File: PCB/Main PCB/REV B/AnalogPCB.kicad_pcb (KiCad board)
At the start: 2 copper layers, 60 x 100 mm, 60 parts, among them J1 DF12NB_4.0_-20DP-0.5V_51_, J2 393570002, J3 393570002, J4 393570002, J5 393570002, J6 SJ3-35053D, Q1 2N7002, Q2 2N7002, Q3 2N7002, U1 ALDP105W, U2 ALDP105W, U3 ALDP105W

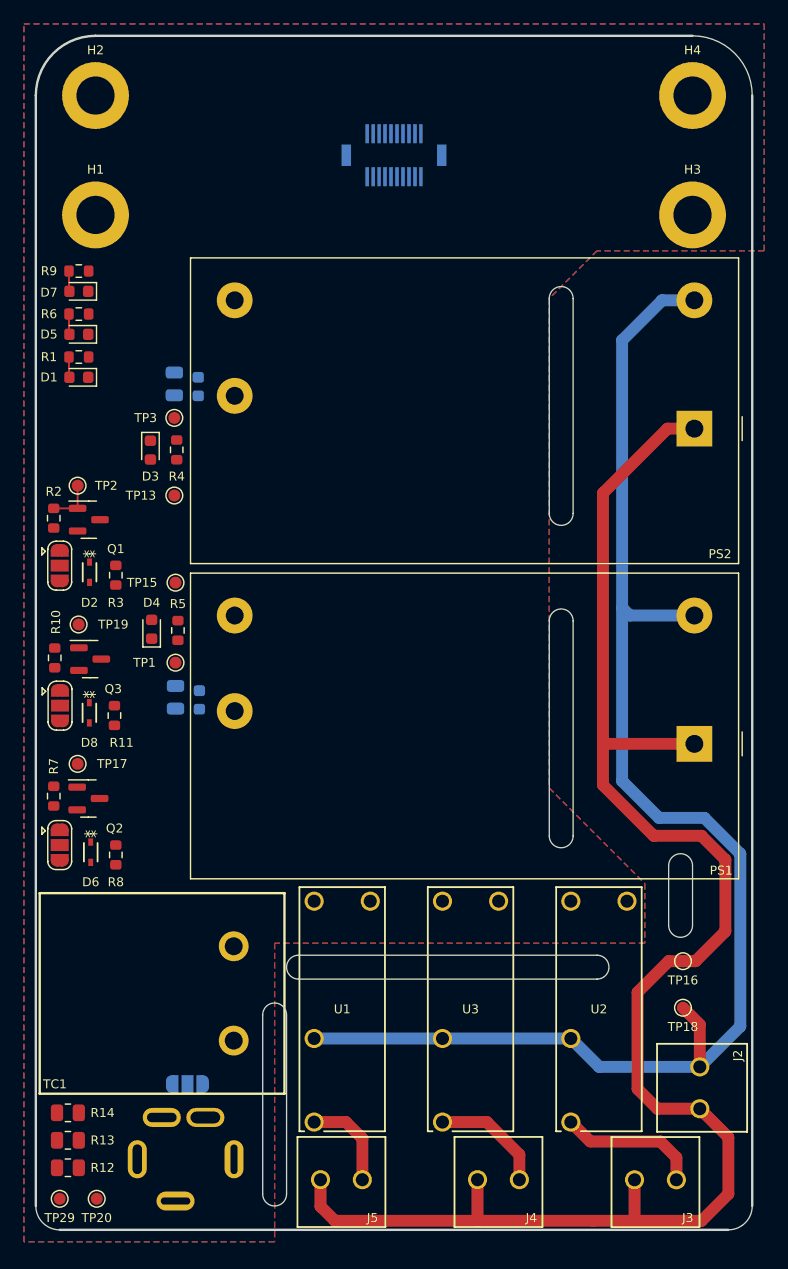
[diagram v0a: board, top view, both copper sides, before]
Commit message: PCB - Analog AC routing half done
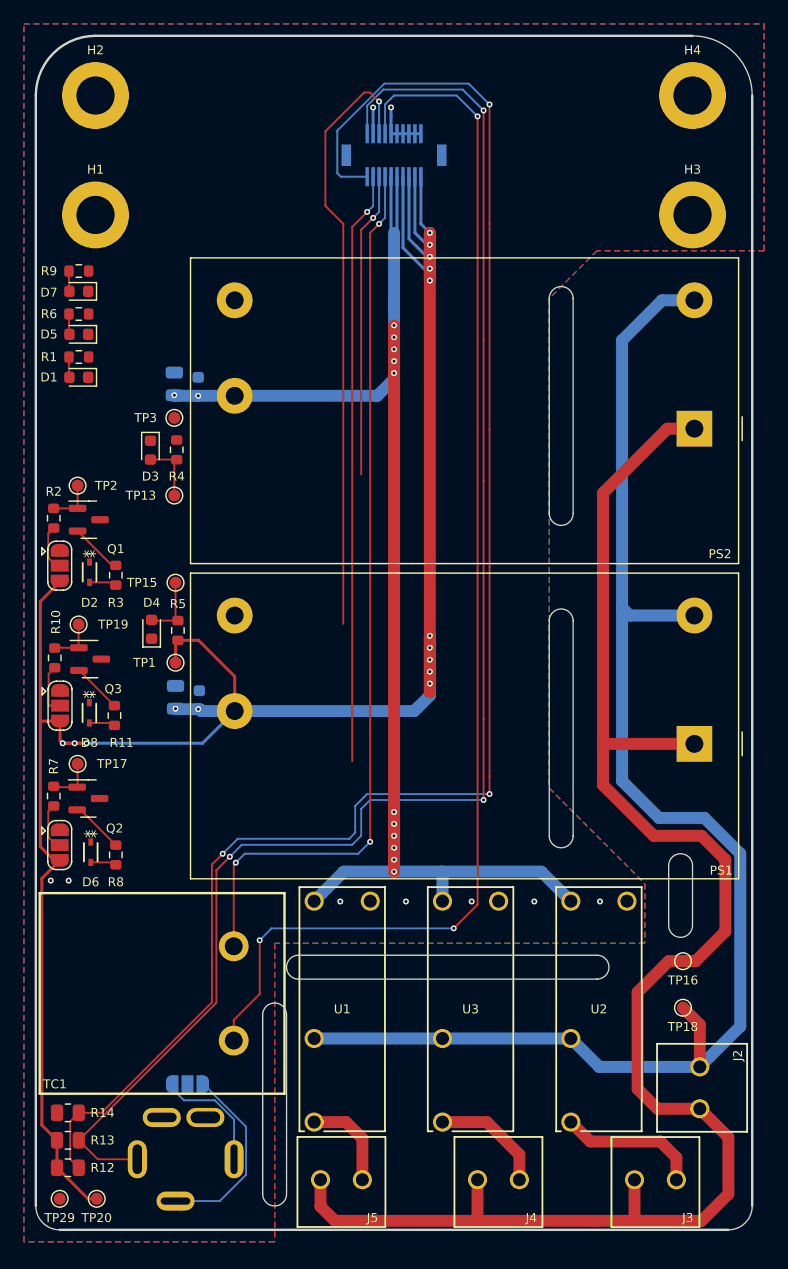
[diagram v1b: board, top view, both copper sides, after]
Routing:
- net +3.3VA: track 0.00 -> 186.8 mm, vias 0 -> 15
- net /MeatProbe+: track 0.00 -> 137.8 mm, vias 0 -> 3
- net /MeatProbe-: track 0.00 -> 130.2 mm, vias 0 -> 3
- net +5V: track 0.00 -> 117.9 mm, vias 0 -> 13
- net /Probe1-: track 0.00 -> 106.0 mm, vias 0 -> 3
- net /Probe1+: track 0.00 -> 75.3 mm, vias 0 -> 3
- net /Opto_Fan: track 0.00 -> 54.7 mm, vias 0 -> 1
- net /Opto_Ignitor: track 0.00 -> 53.6 mm, vias 0 -> 1
- net /Opto_Auger: track 3.90 -> 29.5 mm, vias 0 -> 1
- net /MeatProbeSleeve: track 0.00 -> 15.9 mm
- net /MeatProbeTip: track 0.00 -> 9.96 mm
- net GND: track 0.00 -> 6.90 mm, vias 0 -> 9
- net Net-(D4-Pad2): track 0.00 -> 5.48 mm
- net Net-(D3-Pad2): track 0.00 -> 5.29 mm
- net Net-(D5-Pad1): track 0.00 -> 4.46 mm
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
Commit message: PCB - Analog routing complete, need final review
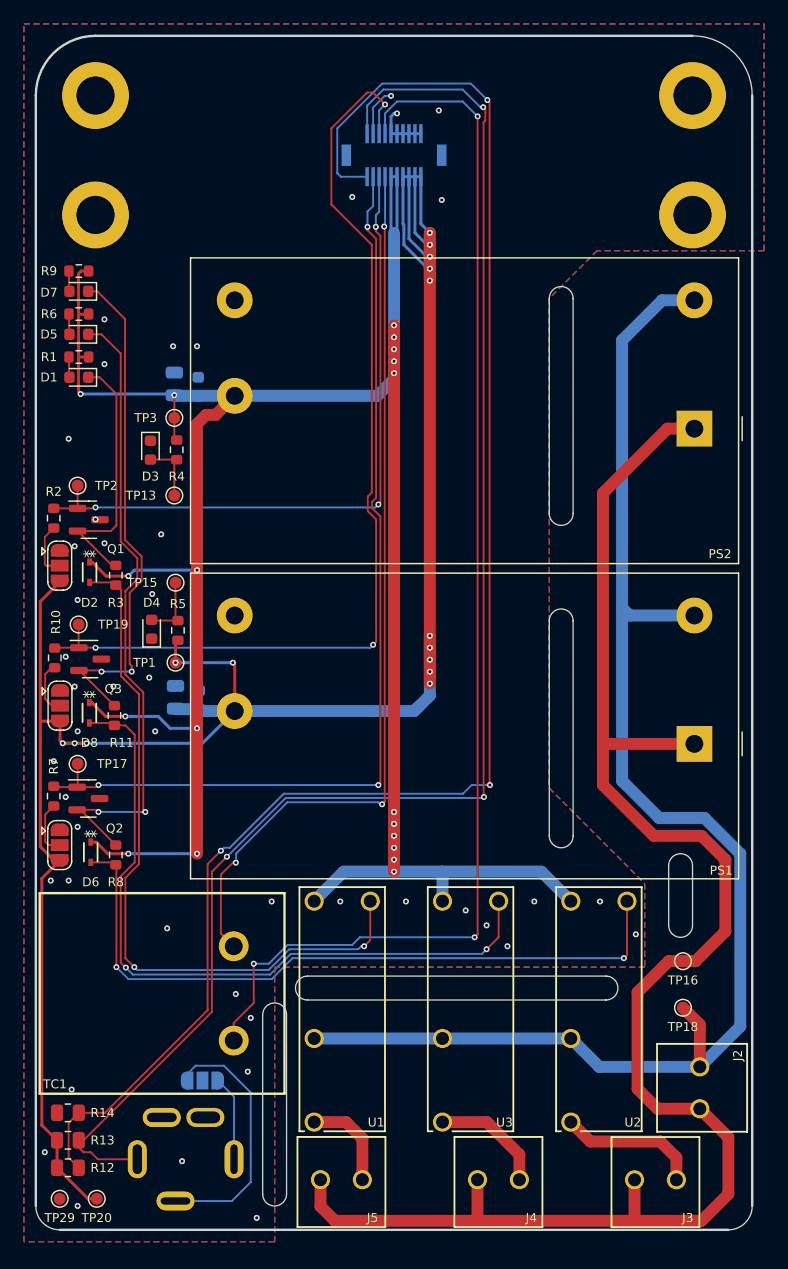
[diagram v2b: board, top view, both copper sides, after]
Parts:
- moved JP4 1.29 mm to (64.0, 137.5), turned to 180 degrees
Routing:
- net +5V: track 117.9 -> 211.3 mm, vias 13 -> 19
- net Net-(D8-Pad2): track 2.18 -> 59.9 mm, vias 0 -> 2
- net Net-(D2-Pad2): track 2.29 -> 59.7 mm, vias 0 -> 2
- net Net-(D6-Pad2): track 2.18 -> 58.9 mm, vias 0 -> 2
- net Net-(D5-Pad1): track 4.46 -> 53.4 mm, vias 0 -> 2
- net Net-(D7-Pad1): track 4.20 -> 43.3 mm, vias 0 -> 2
- net /Opto_Fan: track 54.7 -> 82.7 mm, vias 1 -> 3
- net /Opto_Auger: track 29.5 -> 57.0 mm, vias 1 -> 3
- net /Opto_Ignitor: track 53.6 -> 81.0 mm, vias 1 -> 3
- net Net-(D1-Pad1): track 4.39 -> 21.5 mm
- net /MeatProbeSleeve: track 15.9 -> 21.0 mm
- net /MeatProbeTip: track 9.96 -> 7.15 mm
- net GND: track 6.90 -> 8.66 mm, vias 9 -> 45
- net /MeatProbe-: track 130.2 -> 128.8 mm
- net /MeatProbe+: track 137.8 -> 136.8 mm
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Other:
- outline, holes or cut-outs redrawn

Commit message: PCB - Text edited, all ready for review
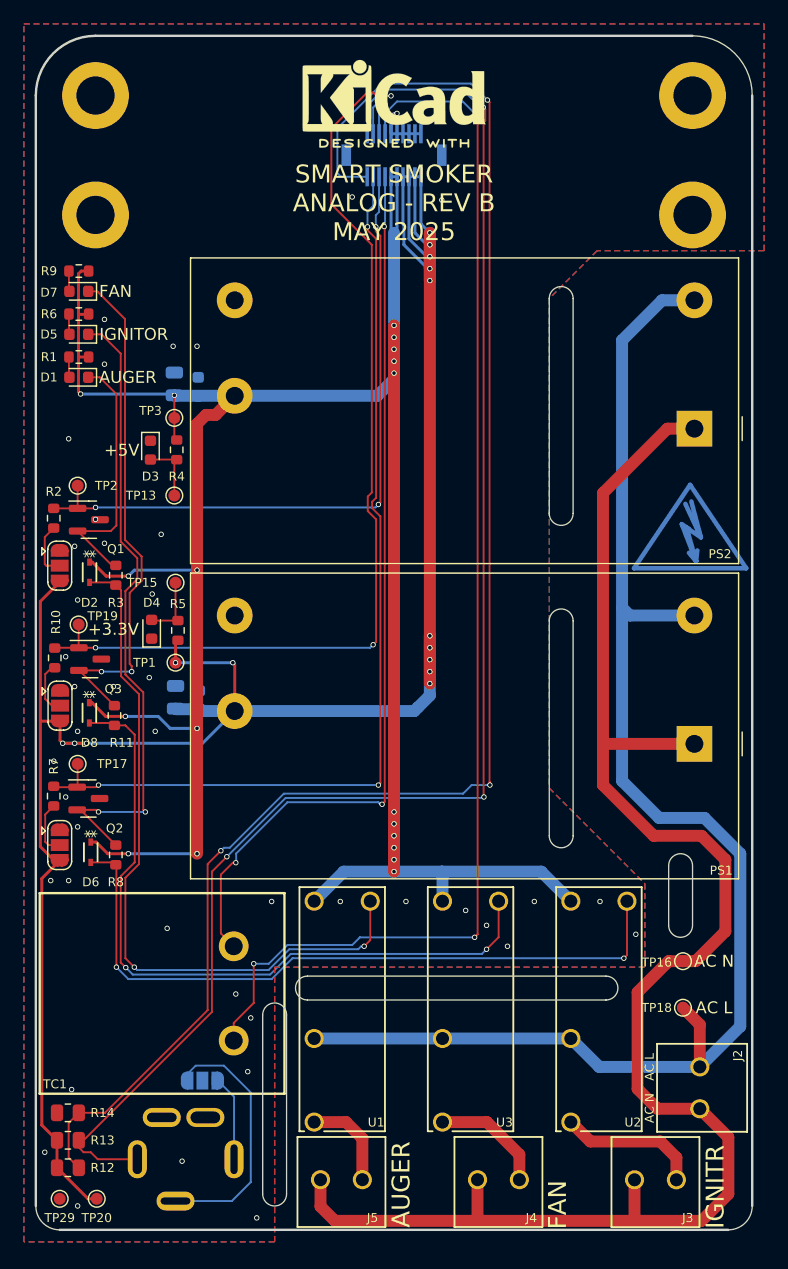
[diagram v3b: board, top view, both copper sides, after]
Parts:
- added REF**: KiCad-Logo2_6mm_SilkScreen, Symbol:KiCad-Logo2_6mm_SilkScreen, F.Cu at (80.0, 55.0)
- added REF**: Symbol_HighVoltage_Type2_CopperTop_VerySmall, Symbol:Symbol_HighVoltage_Type2_CopperTop_VerySmall, B.Cu at (104.8, 91.8)
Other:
- board text added: "+3.3V"
- board text added: "+5V"
- board text added: "AC L"
- board text added: "AC N"
- board text added: "AUGER"
- board text added: "DIMS: 100mm x 60mm HOLE: 10mm x 50mm"
- board text added: "FAN"
- board text added: "IGNITOR"
- board text added: "IGNITR"
- board text added: "SLEEVE"
- board text added: "SMART SMOKER ANALOG - REV B MAY 2025"
- board text added: "TIP"

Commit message: PCB - Analog pcb under review and making minor mods - diode placement
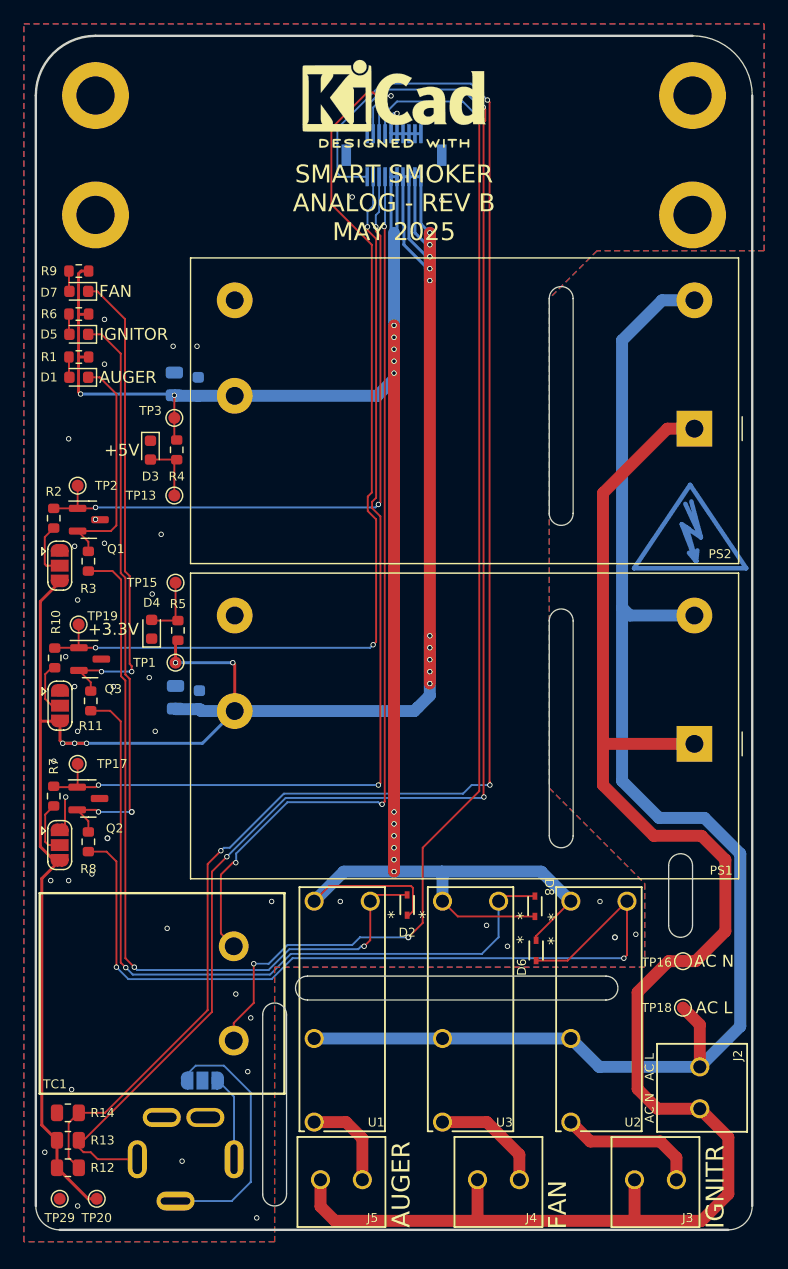
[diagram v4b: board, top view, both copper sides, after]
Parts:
- moved D8 40.7 mm to (91.8, 122.9), turned to 90 degrees
- moved D2 38.5 mm to (81.1, 122.8), turned to 90 degrees
- moved D6 38.2 mm to (91.9, 126.6)
- moved R3 2.58 mm to (54.4, 94.0)
- moved R8 2.55 mm to (54.4, 117.5)
- moved R11 2.33 mm to (54.6, 105.7)
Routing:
- net +5V: track 211.3 -> 166.4 mm, vias 19 -> 13
- net Net-(D6-Pad2): track 58.9 -> 69.7 mm
- net Net-(D5-Pad1): track 53.4 -> 49.0 mm
- net Net-(D2-Pad2): track 59.7 -> 63.4 mm
- net /Probe1-: track 105.8 -> 102.6 mm
- net GND: track 8.66 -> 11.6 mm, vias 45 -> 44
- net Net-(D7-Pad1): track 43.3 -> 40.4 mm
- net Net-(D8-Pad2): track 59.9 -> 62.1 mm, vias 2 -> 1
- net Net-(D1-Pad1): track 21.5 -> 19.5 mm

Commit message: PCB - Analog pcb complete review and gerber generated
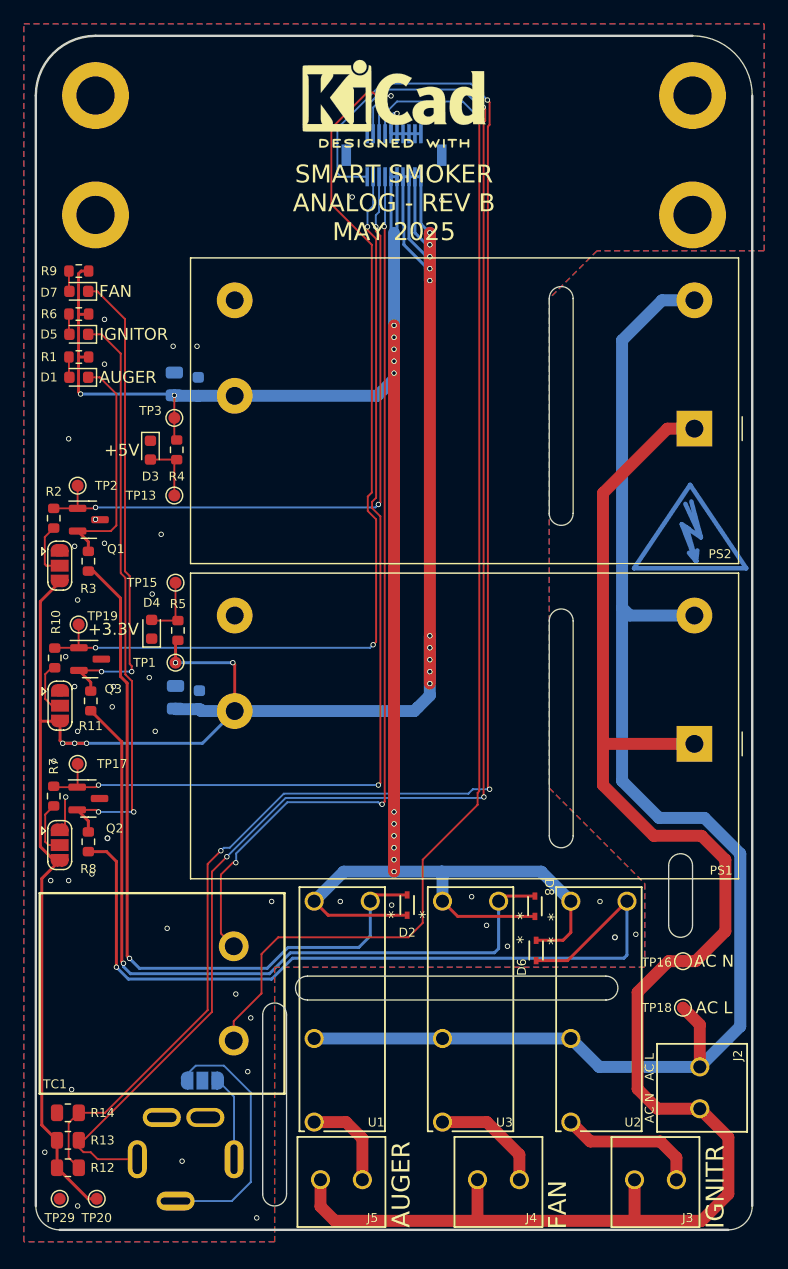
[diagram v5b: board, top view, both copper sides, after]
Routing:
- net +5V: track 166.4 -> 164.6 mm
- net Net-(D2-Pad2): track 63.4 -> 62.0 mm, vias 2 -> 1
- net /Probe1-: track 102.6 -> 102.7 mm, vias 3 -> 1
- net Net-(D6-Pad2): vias 2 -> 1
- net GND: vias 44 -> 47

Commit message: PCB - gerbers generated and boms started
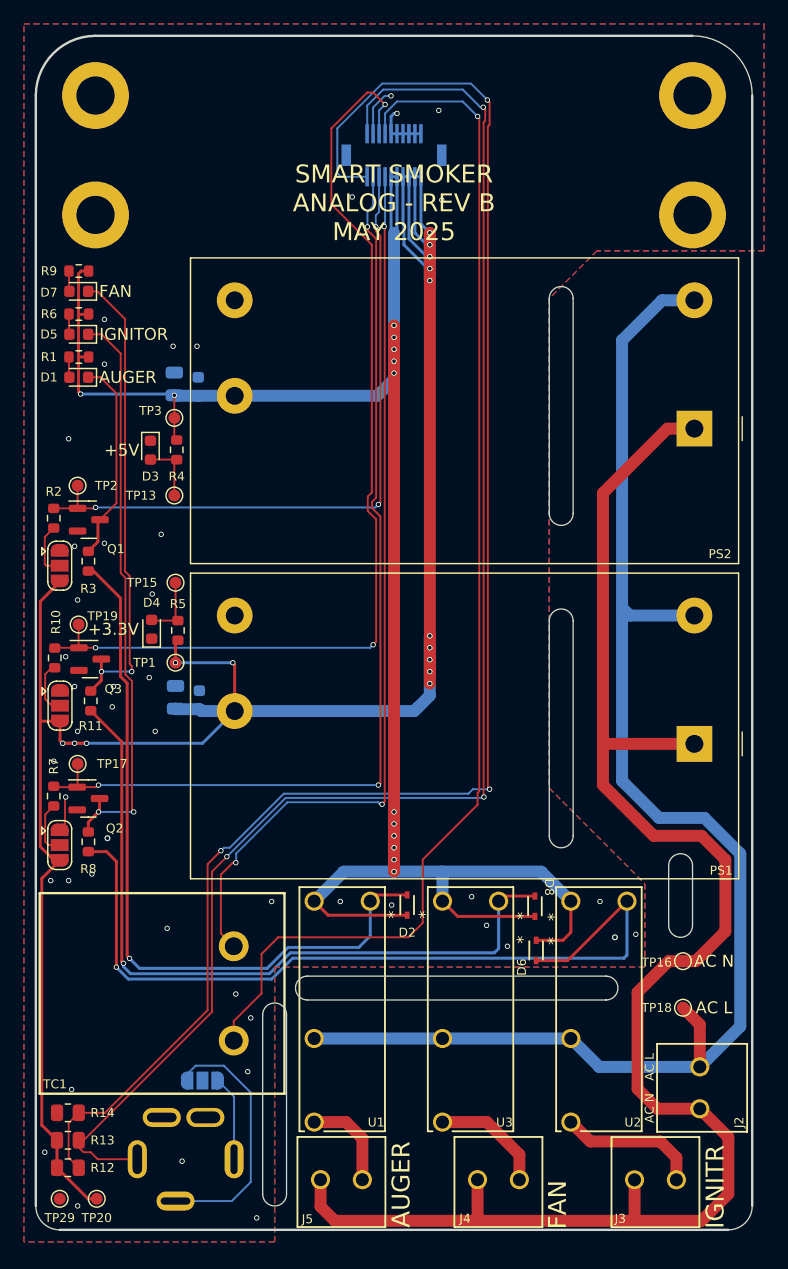
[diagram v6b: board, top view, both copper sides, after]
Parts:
- removed REF**: KiCad-Logo2_6mm_SilkScreen, Symbol:KiCad-Logo2_6mm_SilkScreen
- removed REF**: Symbol_HighVoltage_Type2_CopperTop_VerySmall, Symbol:Symbol_HighVoltage_Type2_CopperTop_VerySmall
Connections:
- Q1 pad 2: Net-(D1-Pad1) -> GND
- Q1 pad 3: GND -> Net-(D1-Pad1)
- Q2 pad 2: Net-(D5-Pad1) -> GND
- Q2 pad 3: GND -> Net-(D5-Pad1)
- Q3 pad 2: Net-(D7-Pad1) -> GND
- Q3 pad 3: GND -> Net-(D7-Pad1)
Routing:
- net Net-(D1-Pad1): track 19.5 -> 16.9 mm
- net Net-(D7-Pad1): track 40.4 -> 39.4 mm
- net Net-(D5-Pad1): track 49.3 -> 48.4 mm
- net GND: vias 47 -> 46
